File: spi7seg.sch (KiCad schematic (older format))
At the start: 47 parts, among them Q1 2N3904BU, Q2 2N3904BU, Q3 2N3904BU, Q4 2N3904BU, Q5 2N3904BU, Q6 2N3904BU, Q7 2N3904BU, Q8 2N3904BU, U1 SN74HC595N, U2 SN74HC161N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

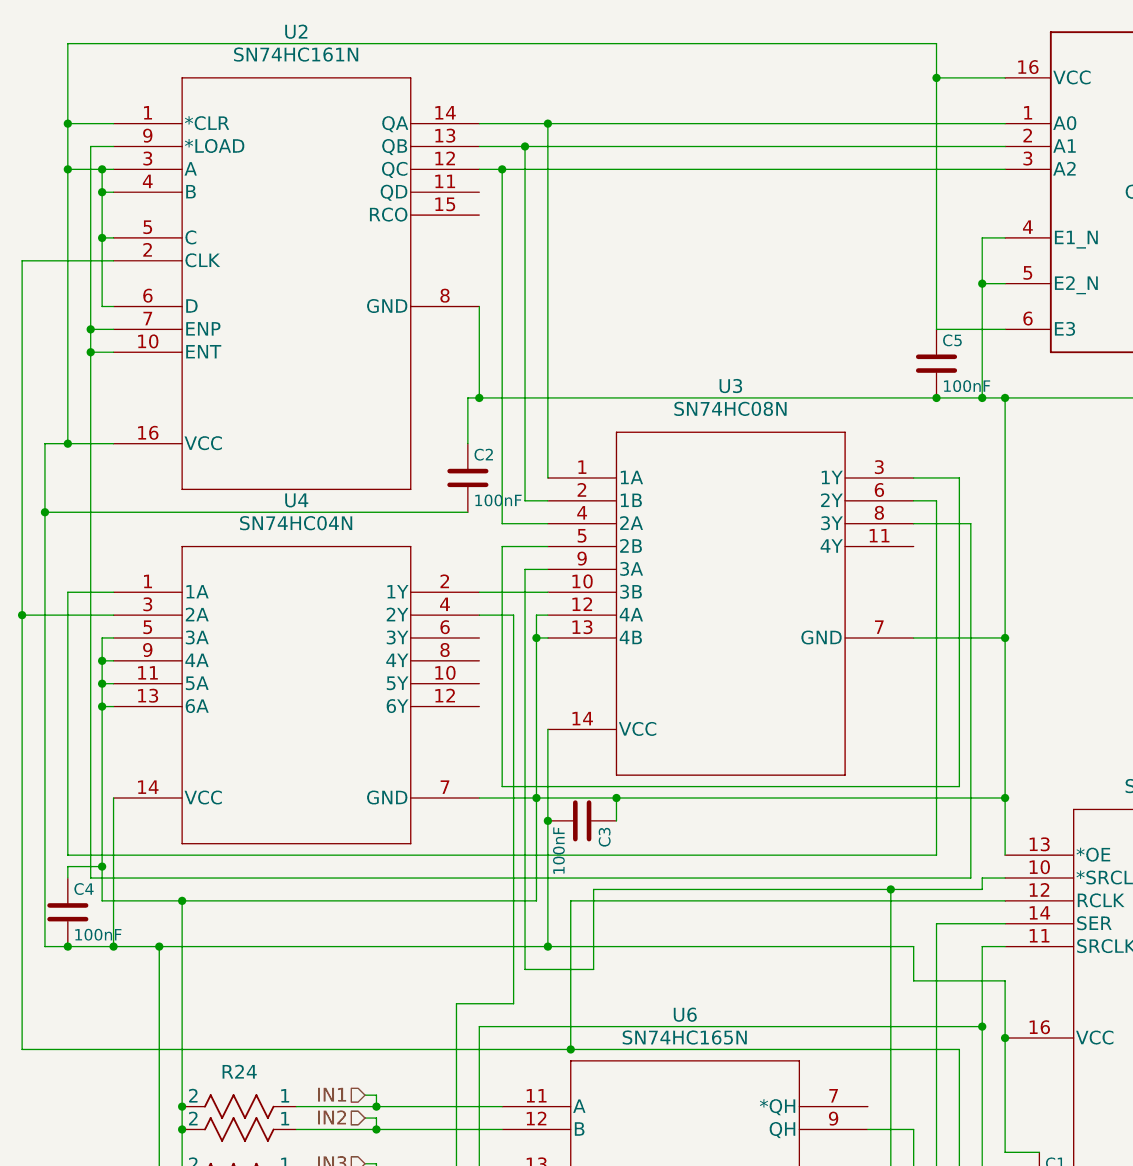
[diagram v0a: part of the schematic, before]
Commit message: Many small improvements.
* Move to V1.1 using less glue logic in the 7-seg display controller.

* Complete perfboard wiring diagram, show in layers.

* Minor spelling error and formatting improvements.
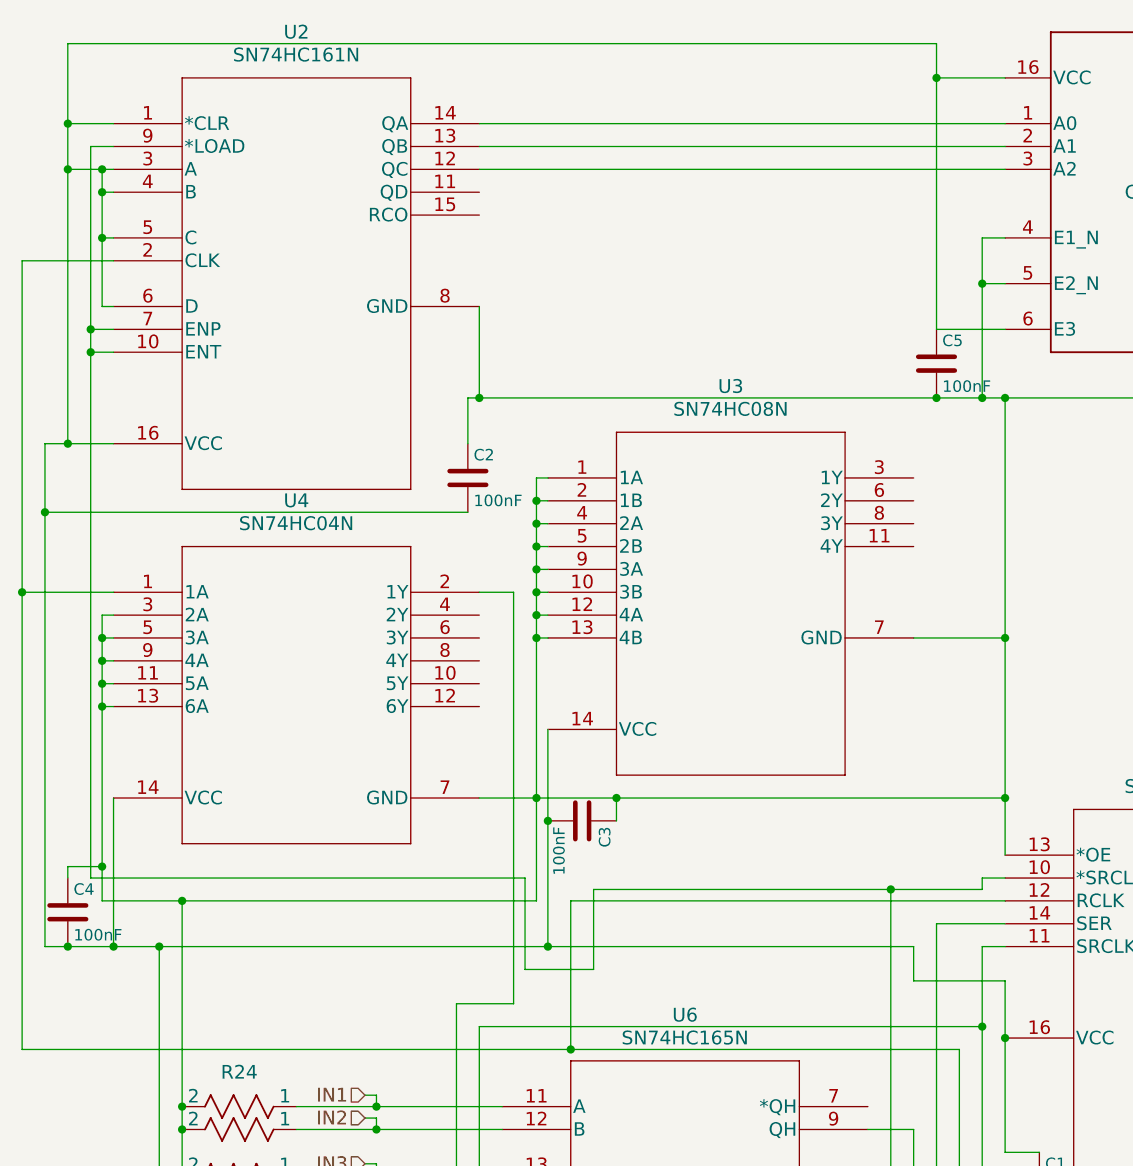
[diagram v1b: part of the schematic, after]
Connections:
- net *RST: now also U2.10 (ENT), U2.7 (ENP), U2.9 (*LOAD); no longer U3.9 (3A)
- net GND: now also U3.1 (1A), U3.10 (3B), U3.2 (1B), U3.4 (2A), U3.5 (2B), U3.9 (3A), U4.3 (2A)
- net SS: now also U4.1 (1A); no longer U4.3 (2A)
- net at U2.14 (QA), U5.1 (A0): no longer U3.1 (1A)
- net at U2.13 (QB), U5.2 (A1): no longer U3.2 (1B)
- net at U2.12 (QC), U5.3 (A2): no longer U3.4 (2A)
- net at U4.2 (1Y): now also U6.1 (SH/*LD); no longer U3.10 (3B)
- net at U3.3 (1Y): no longer U3.5 (2B)
- net at U3.6 (2Y): no longer U4.1 (1A)
- net at U4.4 (2Y): no longer U6.1 (SH/*LD)
- now unconnected: U3.8 (3Y)
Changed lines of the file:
@@
 Title "SPI 7-SEG DPLY KEYPAD CTL DIP"
 Date ""
-Rev "V1"
+Rev "V1.1"
 Comp "Hobbyist Community"
 Comment1 "Designed by quorten"
@@
 	4500 4500 4500 6250
 Wire Wire Line
-	2700 2950 2700 4700
+	2700 4300 2700 4700
 Wire Wire Line
 	4700 4300 4800 4300
@@
 	850  3350 900  3350
 Wire Wire Line
-	850  4400 850  3250
+	850  4400 850  3150
 Wire Wire Line
 	850  3250 900  3250
@@
 	2750 3250 2800 3250
 Wire Wire Line
-	2750 3150 2750 4400
+	2750 2550 2750 4400
 Wire Wire Line
 	2750 3150 2800 3150
 Wire Wire Line
-	2650 3150 2650 4850
-Wire Wire Line
-	2500 3150 2650 3150
-Connection ~ 500  3150
+	2650 3050 2650 4850
+Connection ~ 500  3050
 Wire Wire Line
 	500  5050 4600 5050
-Wire Wire Line
-	500  3150 900  3150
 Wire Wire Line
 	500  1600 500  5050
@@
 Wire Wire Line
 	4400 3250 4800 3250
-Wire Wire Line
-	800  4300 4650 4300
-Wire Wire Line
-	2800 2950 2700 2950
-Wire Wire Line
-	2500 3050 2800 3050
-Wire Wire Line
-	700  3050 900  3050
-Wire Wire Line
-	700  4200 700  3050
-Wire Wire Line
-	2600 2850 2800 2850
 Connection ~ 6400 2200
 Wire Wire Line
 	2500 1800 2500 2200
 Wire Wire Line
-	4400 2750 4650 2750
-Wire Wire Line
-	4500 2650 4400 2650
-Wire Wire Line
-	4500 4200 700  4200
-Wire Wire Line
-	4500 2650 4500 4200
-Wire Wire Line
-	2600 3900 2600 2850
-Connection ~ 2600 1200
-Connection ~ 2700 1100
-Connection ~ 2800 1000
-Wire Wire Line
-	4650 2750 4650 4300
-Wire Wire Line
-	4600 3900 2600 3900
-Wire Wire Line
-	4600 2550 4600 3900
-Wire Wire Line
-	4400 2550 4600 2550
-Wire Wire Line
-	2600 2750 2800 2750
-Wire Wire Line
-	2600 1200 2600 2750
-Wire Wire Line
 	2500 1200 4800 1200
 Wire Wire Line
-	2700 2650 2800 2650
-Wire Wire Line
-	2700 1100 2700 2650
-Wire Wire Line
 	2500 1100 4800 1100
 Wire Wire Line
 	2500 1000 4800 1000
-Wire Wire Line
-	2800 2550 2800 1000
 Wire Wire Line
 	7000 4900 9550 4900
@@
 	7300 4100 7300 4900
 Connection ~ 7300 4900
+Wire Wire Line
+	2650 3050 2500 3050
+Wire Wire Line
+	500  3050 900  3050
+Wire Wire Line
+	850  3150 900  3150
+Connection ~ 850  3250
+Wire Wire Line
+	2750 3050 2800 3050
+Connection ~ 2750 3150
+Wire Wire Line
+	2750 2950 2800 2950
+Connection ~ 2750 3050
+Wire Wire Line
+	2750 2850 2800 2850
+Connection ~ 2750 2950
+Wire Wire Line
+	2750 2750 2800 2750
+Connection ~ 2750 2850
+Wire Wire Line
+	2750 2650 2800 2650
+Connection ~ 2750 2750
+Wire Wire Line
+	2750 2550 2800 2550
+Connection ~ 2750 2650
+Wire Wire Line
+	800  4300 2700 4300
 $EndSCHEMATC
